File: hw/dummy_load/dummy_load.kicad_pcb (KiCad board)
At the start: 4 copper layers, 100 x 87 mm, 116 parts, among them J1 12V optional, J10 Calib gain, J11 Calib divider, J12 12V in, J2 NTC DUT, J3 NTC Ambient, J4 NTC Heatsink, J5 Fan1, J6 Fan2, J7 NTC Heatsink, J8 NTC Heatsink, J9 NTC Heatsink, Q1 DMN2056U, Q10 DMG2305UX-7, Q2 IRL540NPBF, Q3 IRL540NPBF, Q4 IRL540NPBF, Q5 IRL540NPBF, Q6 IRL540NPBF, Q7 IRL540NPBF, Q8 IRL540NPBF, Q9 IRL540NPBF, U1 LM358, U2 AD620, U21 LM4040B30FTA, U3 LM4040B30FTA, U5 74HC4051, U6 AD5272BCP, U7 AD5272BCP, U8 AMS1117-5.0, X1 WAGO 2604-1102

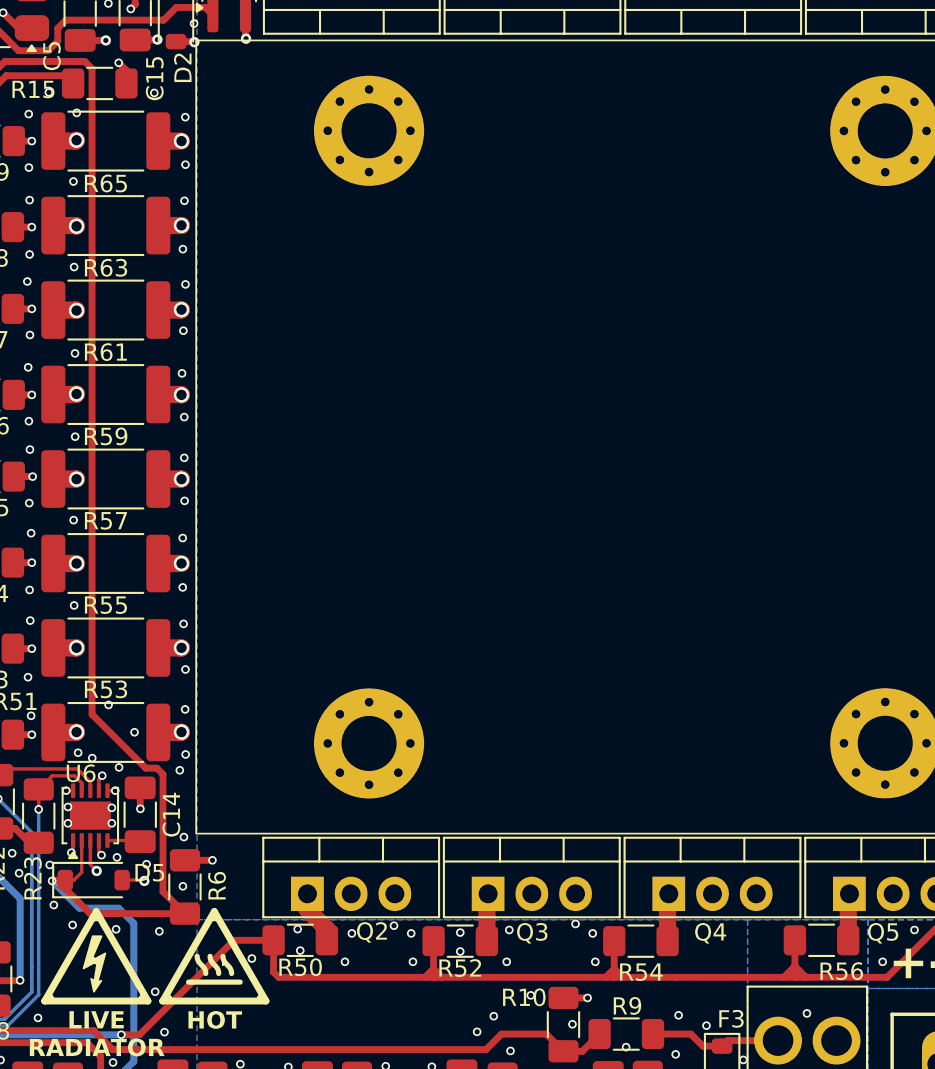
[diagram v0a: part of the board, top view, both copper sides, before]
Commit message: Add more vias
Signed-off-by: Mateusz Pajak <22417805+Tai-Min@users.noreply.github.com>
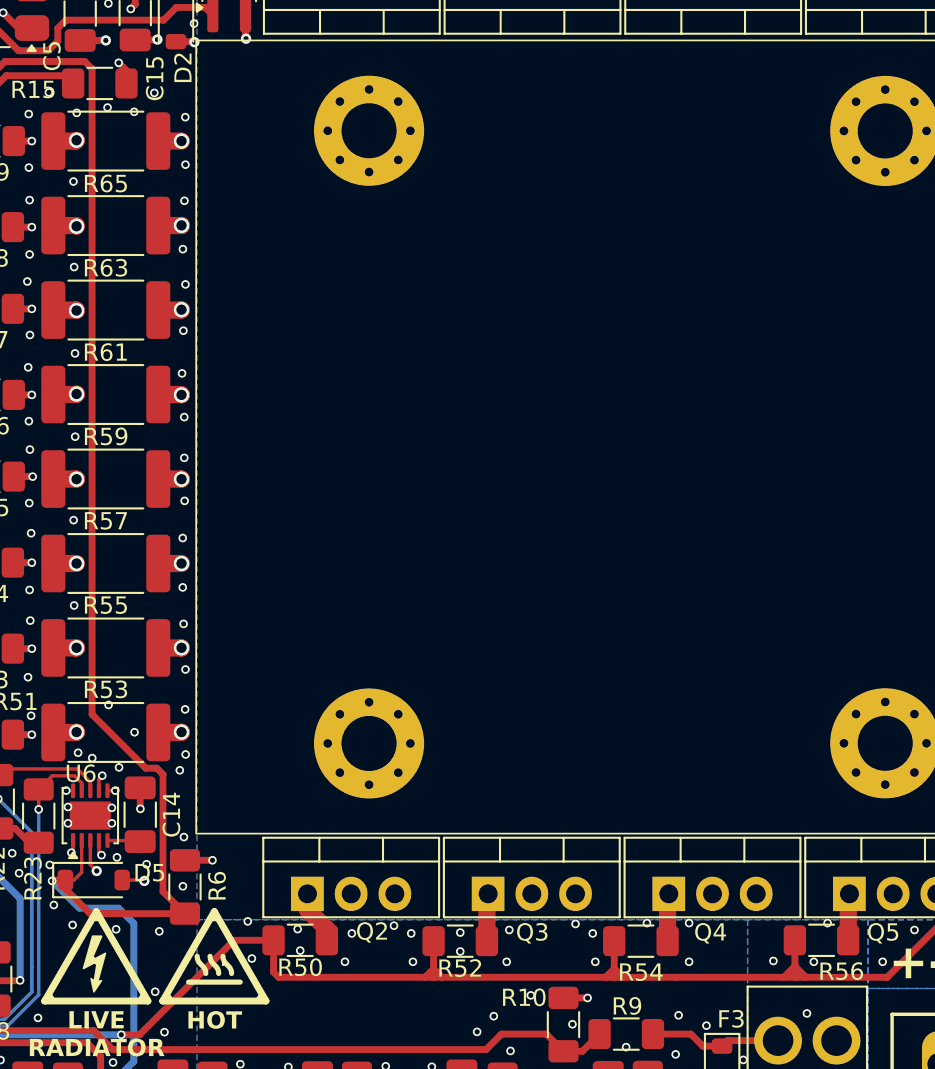
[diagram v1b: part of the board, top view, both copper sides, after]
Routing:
- net GND: vias 466 -> 475
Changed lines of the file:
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@@
 	)
 	(via
+		(at 180.6 111.95)
+		(size 0.5)
+		(drill 0.3)
+		(layers "F.Cu" "B.Cu")
+		(free yes)
+		(net 4)
+	)
+	(via
 		(at 107.25 118.51)
 		(size 0.5)
@@
 	)
 	(via
+		(at 143.45 62.6)
+		(size 0.5)
+		(drill 0.3)
+		(layers "F.Cu" "B.Cu")
+		(net 4)
+	)
+	(via
 		(at 128.85 48.75)
 		(size 0.5)
@@
 	)
 	(via
+		(at 182.95 112)
+		(size 0.5)
+		(drill 0.3)
+		(layers "F.Cu" "B.Cu")
+		(free yes)
+		(net 4)
+	)
+	(via
 		(at 139.93 86.33)
 		(size 0.5)
@@
 	)
 	(via
+		(at 173.25 109.75)
+		(size 0.5)
+		(drill 0.3)
+		(layers "F.Cu" "B.Cu")
+		(free yes)
+		(net 4)
+	)
+	(via
 		(at 127.4 117.8)
 		(size 0.5)
@@
 	)
 	(via
+		(at 175.7 112)
+		(size 0.5)
+		(drill 0.3)
+		(layers "F.Cu" "B.Cu")
+		(free yes)
+		(net 4)
+	)
+	(via
 		(at 169.4 122.6)
 		(size 0.5)
@@
 	)
 	(via
+		(at 141.9 62.35)
+		(size 0.5)
+		(drill 0.3)
+		(layers "F.Cu" "B.Cu")
+		(net 4)
+	)
+	(via
 		(at 197.75 103.75)
 		(size 0.5)
@@
 	)
 	(via
+		(at 175.7 109.75)
+		(size 0.5)
+		(drill 0.3)
+		(layers "F.Cu" "B.Cu")
+		(free yes)
+		(net 4)
+	)
+	(via
 		(at 101.54 61.18)
 		(size 0.5)
@@
 	)
 	(via
+		(at 150.05 109.65)
+		(size 0.5)
+		(drill 0.3)
+		(layers "F.Cu" "B.Cu")
+		(free yes)
+		(net 4)
+	)
+	(via
 		(at 137.46 87.09)
 		(size 0.5)
@@
 	)
 	(via
+		(at 183.75 109.75)
+		(size 0.5)
+		(drill 0.3)
+		(layers "F.Cu" "B.Cu")
+		(free yes)
+		(net 4)
+	)
+	(via
 		(at 104.7 106.8)
 		(size 0.5)
@@
 	)
 	(zone
+		(net 0)
+		(net_name "")
+		(layer "F.Cu")
+		(hatch edge 0.5)
+		(connect_pads
+			(clearance 0)
+		)
+		(min_thickness 0.25)
+		(filled_areas_thickness no)
+		(keepout
+			(tracks allowed)
+			(vias allowed)
+			(pads allowed)
+			(copperpour not_allowed)
+			(footprints allowed)
+		)
+		(placement
+			(enabled no)
+			(sheetname "")
+		)
+		(fill
+			(thermal_gap 0.5)
+			(thermal_bridge_width 0.5)
+		)
+		(polygon
+			(pts
+				(xy 116.55 113.45) (xy 114.95 113.45) (xy 114.95 115.5) (xy 116.55 115.5)
+			)
+		)
+	)
+	(zone

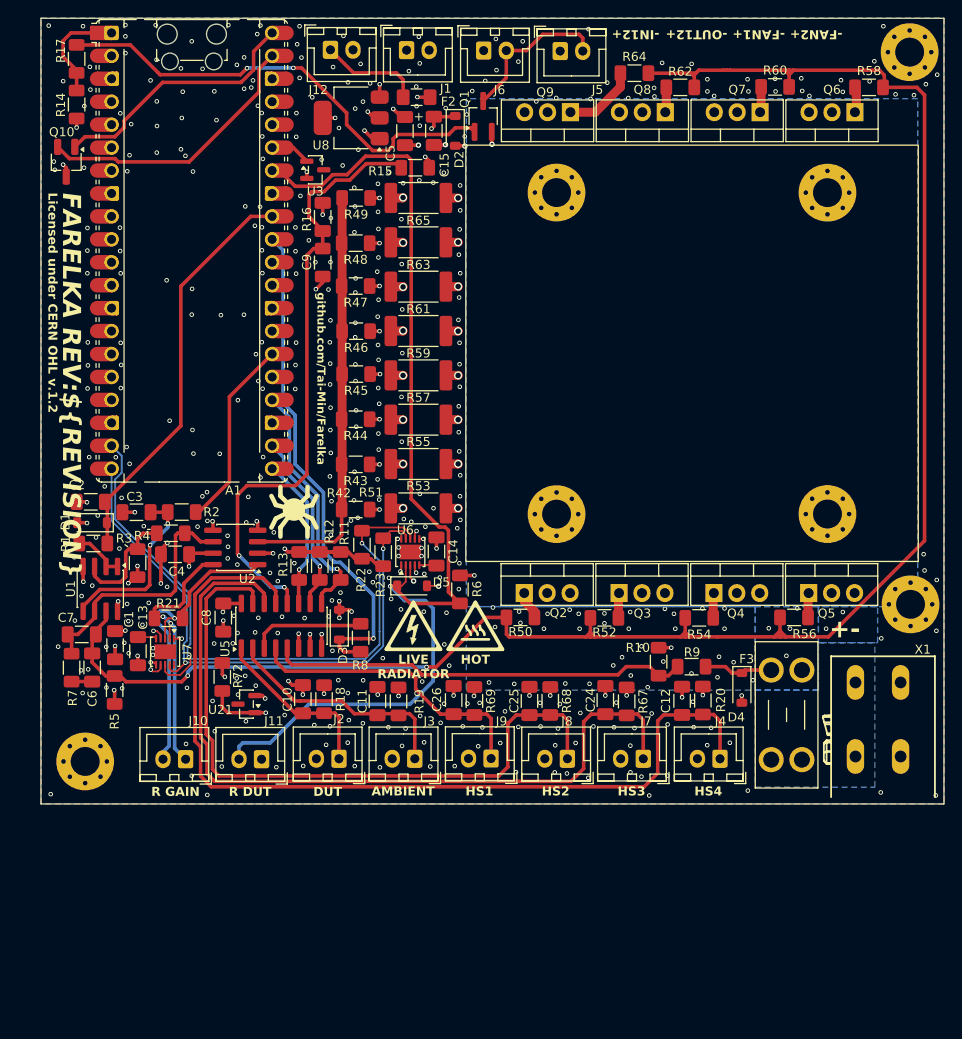
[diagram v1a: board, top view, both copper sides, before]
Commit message: Better PCB design, update BOM, add UART header for debugging (#7)
Signed-off-by: Mateusz Pajak <22417805+Tai-Min@users.noreply.github.com>
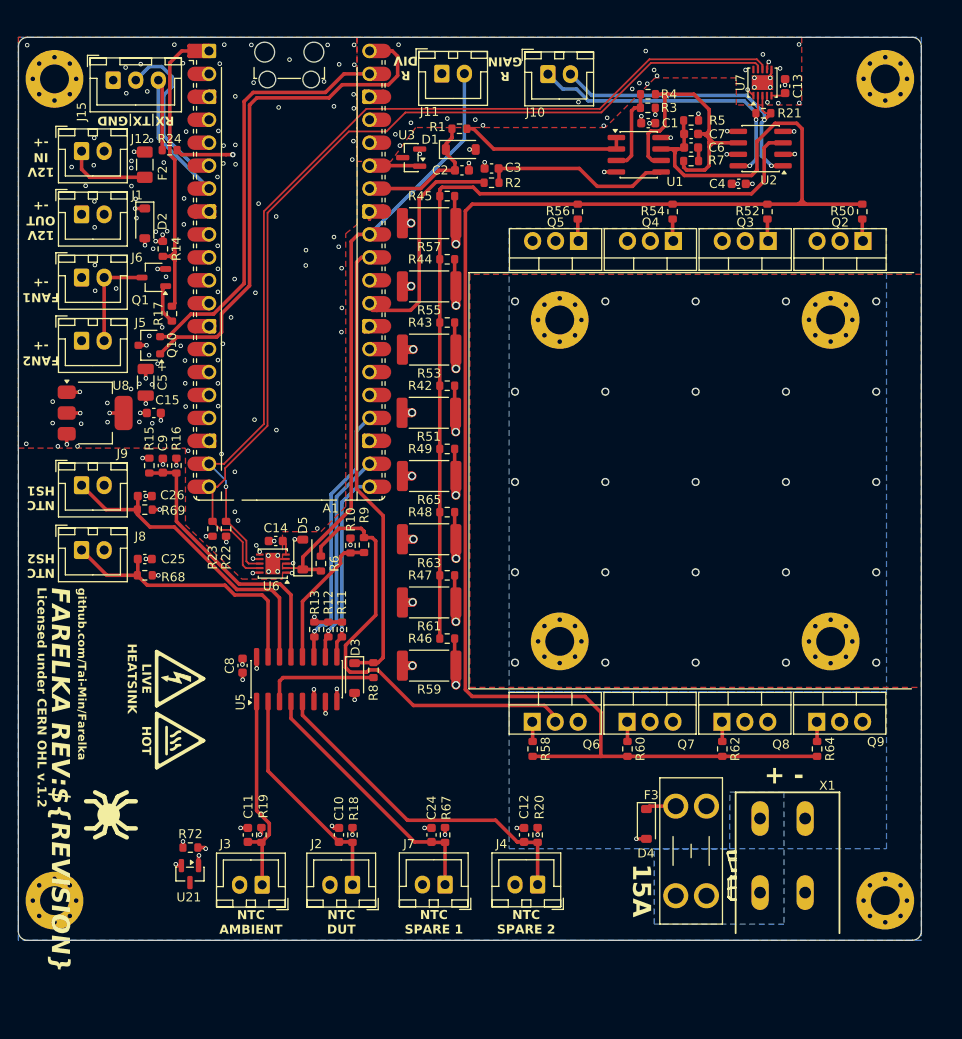
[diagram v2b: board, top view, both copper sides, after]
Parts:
- added H2: MountingHole, MountingHole:MountingHole_3.2mm_M3_Pad_Via, F.Cu at (193.5, 51.1)
- added J15: Conn_01x03, Connector_JST:JST_XH_B3B-XH-A_1x03_P2.50mm_Vertical, F.Cu at (108.0, 51.2)
- added R24: 10K, Resistor_SMD:R_0603_1608Metric, F.Cu at (114.2, 59.0)
- C1, C10, C11, C12, C13, C14, C15, C2, C24, C25, C26, C3, C4, C6, C7, C8, C9: footprint Capacitor_SMD:C_1206_3216Metric_Pad1.33x1.80mm_HandSolder -> Capacitor_SMD:C_0603_1608Metric
- C5: footprint Capacitor_SMD:C_1206_3216Metric_Pad1.33x1.80mm_HandSolder -> Capacitor_SMD:C_1206_3216Metric
- F2: value BORN SMD1206-100/06N -> 1206L300SL16ARG; footprint Fuse:Fuse_1206_3216Metric_Pad1.42x1.75mm_HandSolder -> Fuse:Fuse_1206_3216Metric
- J4, J7: value NTC Heatsink -> NTC Spare
- Q1: footprint Package_TO_SOT_SMD:TSOT-23_HandSoldering -> Package_TO_SOT_SMD:TSOT-23
- Q10: footprint Package_TO_SOT_SMD:SC-59_Handsoldering -> Package_TO_SOT_SMD:SC-59
- R1, R10, R11, R12, R13, R14, R15, R16, R17, R18, R19, R2, R20, R21, R22, R23, R3, R4, R42, R43, R44, R45, R46, R47, R48, R49, R5, R50, R52, R54, R56, R58, R60, R62, R64, R67, R68, R69, R7, R72, R8, R9: footprint Resistor_SMD:R_1206_3216Metric_Pad1.30x1.75mm_HandSolder -> Resistor_SMD:R_0603_1608Metric
- R51, R53, R55, R57, R59, R61, R63, R65: footprint Resistor_SMD:R_2512_6332Metric_Pad1.40x3.35mm_HandSolder -> Resistor_SMD:R_2512_6332Metric
- R6: value 8.06K -> 8.06K 1%; footprint Resistor_SMD:R_1206_3216Metric_Pad1.30x1.75mm_HandSolder -> Resistor_SMD:R_0603_1608Metric
- moved H3 100.3 mm to (101.5, 142.1)
- moved C13 95.1 mm to (182.4, 51.9), turned to -90 degrees
- moved H1 94.7 mm to (101.5, 51.1)
- moved U7 91.4 mm to (179.9, 51.5), turned to 90 degrees
- moved H4 89.9 mm to (193.5, 142.1)
- moved R5 89.7 mm to (172.0, 55.7), turned to 180 degrees
- moved R7 88.6 mm to (172.0, 60.2), turned to 0 degrees
- moved C6 87.8 mm to (172.0, 58.7), turned to 0 degrees
- moved C7 87.3 mm to (172.0, 57.2), turned to 0 degrees
- moved R21 86.4 mm to (180.0, 54.9)
- moved J10 85.8 mm to (156.1, 50.6), turned to 0 degrees
- moved C1 82.6 mm to (167.2, 56.0), turned to 0 degrees
- moved R58 82.2 mm to (154.4, 125.3), turned to -90 degrees
- moved J11 78.5 mm to (144.4, 50.5), turned to 0 degrees
- moved R64 77.5 mm to (185.9, 125.3), turned to -90 degrees
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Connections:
- A1 pad 21: /MUX_S0 -> /MUX_S2
- A1 pad 24: /MUX_S2 -> /MUX_S0
- A1 pad 26: /LOAD_CTRL -> unconnected-(A1-GPIO20-Pad26)_1
- A1 pad 29: unconnected-(A1-GPIO22-Pad29) -> /LOAD_CTRL
- A1 pad 32: /LOAD_FEEDBACK -> /DUT_SENSE_PRECISE
- A1 pad 33: GND -> GNDA
- A1 pad 34: /DUT_SENSE_PRECISE -> /LOAD_FEEDBACK
- A1 pad 6: unconnected-(A1-GPIO4-Pad6)_1 -> /UART_TX
- A1 pad 7: unconnected-(A1-GPIO5-Pad7)_1 -> /UART_RX
- C1 pad 1: GND -> GNDA
- C10 pad 1: GND -> GNDA
- C11 pad 1: GND -> GNDA
- C12 pad 1: GND -> GNDA
- C12 pad 2: /NTC_HEATSINK_4 -> /NTC_SPARE_2
- C2 pad 1: GND -> GNDA
- C24 pad 1: GND -> GNDA
- C24 pad 2: /NTC_HEATSINK_3 -> /NTC_SPARE_1
- C25 pad 1: GND -> GNDA
- C26 pad 1: GND -> GNDA
- C3 pad 1: GND -> GNDA
- C4 pad 1: GND -> GNDA
- C8 pad 1: GND -> GNDA
- C9 pad 1: GND -> GNDA
- C9 pad 2: Net-(U5-A3) -> Net-(U5-A0)
- D1 pad 2: GND -> GNDA
- D3 pad 2: GND -> GNDA
- D4 pad 2: GND -> GNDA
- D5 pad 2: GND -> GNDA
- H1 pad 1: (no net) -> GND
- H3 pad 1: (no net) -> GND
- H4 pad 1: (no net) -> GND
- J11 pad 1: GND -> GNDA
- J2 pad 2: GND -> GNDA
- J3 pad 2: GND -> GNDA
- J4 pad 1: /NTC_HEATSINK_4 -> /NTC_SPARE_2
- J4 pad 2: GND -> GNDA
- J7 pad 1: /NTC_HEATSINK_3 -> /NTC_SPARE_1
- J7 pad 2: GND -> GNDA
- J8 pad 2: GND -> GNDA
- J9 pad 2: GND -> GNDA
- R10 pad 1: GND -> GNDA
- R15 pad 1: Net-(U5-A3) -> Net-(U5-A0)
- R16 pad 1: GND -> GNDA
- R16 pad 2: Net-(U5-A3) -> Net-(U5-A0)
- R20 pad 2: /NTC_HEATSINK_4 -> /NTC_SPARE_2
- R3 pad 1: GND -> GNDA
- R5 pad 1: GND -> GNDA
- R51 pad 2: GND -> GNDA
- R53 pad 2: GND -> GNDA
- R55 pad 2: GND -> GNDA
- R57 pad 2: GND -> GNDA
- R59 pad 2: GND -> GNDA
- R61 pad 2: GND -> GNDA
- R63 pad 2: GND -> GNDA
- R65 pad 2: GND -> GNDA
- R67 pad 2: /NTC_HEATSINK_3 -> /NTC_SPARE_1
- U1 pad 4: GND -> GNDA
- U2 pad 2: GND -> GNDA
- U2 pad 4: GND -> GNDA
- U2 pad 5: GND -> GNDA
- U21 pad 2: GND -> GNDA
- U3 pad 2: GND -> GNDA
- U5 pad 1: /NTC_DUT -> /NTC_AMBIENT
- U5 pad 12: Net-(U5-A3) -> /DUT_SENSE
- U5 pad 13: /NTC_HEATSINK_4 -> Net-(U5-A0)
- U5 pad 14: /NTC_HEATSINK_3 -> /NTC_HEATSINK_1
- U5 pad 2: /NTC_AMBIENT -> /NTC_DUT
- U5 pad 4: /NTC_HEATSINK_1 -> /NTC_SPARE_1
- U5 pad 5: /DUT_SENSE -> /NTC_SPARE_2
- U5 pad 7: GND -> GNDA
- U6 pad 3: GND -> GNDA
- X1 pad P1.1: GND -> GNDA
- X1 pad P1.2: GND -> GNDA
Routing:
- net /NTC_HEATSINK_4: track 101.3 -> 0.00 mm
- net /NTC_HEATSINK_3: track 88.5 -> 0.00 mm
- net Net-(U5-A3): track 68.4 -> 0.00 mm, vias 2 -> 0
- net GND: track 72.3 -> 15.0 mm, vias 475 -> 145
- net /DUT_SENSE_PRECISE: track 120.1 -> 67.1 mm, vias 1 -> 0
- net Net-(Q1-G): track 52.0 -> 4.43 mm, vias 2 -> 0
- net /load/LOAD_FEEDBACK: track 47.1 -> 92.6 mm
- net /NTC_HEATSINK_2: track 76.0 -> 31.0 mm
- net /LOAD: track 9.29 -> 54.0 mm, vias 1 -> 25
- net /DIGIPOT_SCL: track 65.9 -> 108.2 mm, vias 2 -> 0
- net /NTC_SPARE_2: track 0.00 -> 38.1 mm
- net /DIGIPOT_SDA: track 74.5 -> 108.6 mm, vias 2 -> 1
- net GNDA: track 0.00 -> 33.8 mm, vias 0 -> 36
- net /LOAD_FEEDBACK: track 45.4 -> 13.8 mm
- net Net-(U5-A0): track 0.00 -> 31.3 mm
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- added copper zone on F.Cu, net /LOAD
- added copper zone on In1.Cu, net /LOAD
- added copper zone on In2.Cu, net GNDA
- added copper zone on In1.Cu, net Net-(F3-Pad2)
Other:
- board size 100 x 87 mm -> 100 x 100 mm
- board text added: "+ -"
- board text added: "12V IN -+"
- board text added: "12V OUT -+"
- board text added: "15A"
- board text added: "FAN1 -+"
- board text added: "FAN2 -+"
- board text added: "LIVE HEATSINK"
- board text added: "NTC AMBIENT"
- board text added: "NTC DUT"
- board text added: "NTC HS1"
- board text added: "NTC HS2"
- board text added: "NTC SPARE 1"
- board text added: "NTC SPARE 2"
- board text added: "R DIV"
- board text added: "RX|TX|GND"
- board text removed: "+"
- board text removed: "+-"
- board text removed: "-FAN1+"
- board text removed: "-FAN2+"
- board text removed: "-IN12+"
- board text removed: "-OUT12+"
- board text removed: "AMBIENT"
- board text removed: "DUT"
- board text removed: "HS1"
- board text removed: "HS2"
- board text removed: "HS3"
- board text removed: "HS4"
- board text removed: "LIVE RADIATOR"
- board text removed: "R DUT"
